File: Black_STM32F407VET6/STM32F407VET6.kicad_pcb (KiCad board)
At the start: 2 copper layers, 100 x 100 mm, 89 parts, among them J1 T0, J10 - HotBed +, J11 Heater0, J12 X-, J13 Y-, J14 Z-, J15 Z+, J16 USB_B, J17 LeftSpi, J18 EXTRAPINS, J19 12Vinput, J2 T1, J20 5VOut, J23 EXP2, J24 LCD2004, J25 Bottom, J26 Right, J28 LIGHTS, J29 Z, J3 TB, J30 Z, J38 X, J39 Y, J4 TC, J41 E0, J43 Heater1, J44 COM, J47 I2C, J48 SPI, J49 SPI, J5 + VIN -, J50 SDIO, J51 Servo, J52 Servo, J53 PowerSelect, J54 Power, J55 PD11, J56 Power, J6 Fan3, J7 Fan2, J8 Fan1, J9 Fan0, Q12 IRLR8726PBF, Q13 IRLR8726PBF, Q14 IRLR8726PBF, Q4 IRLML0030TRPBF, Q6 IRLML0030TRPBF, Q7 IRLML0030TRPBF, Q8 IRLML0030TRPBF, SW1 Boot0, U1 LeftAnalog, U2 Left5V, U3 BuckConvertor, U4 LM2901, U5 AT24CS01-SSHM, U6 LM2901

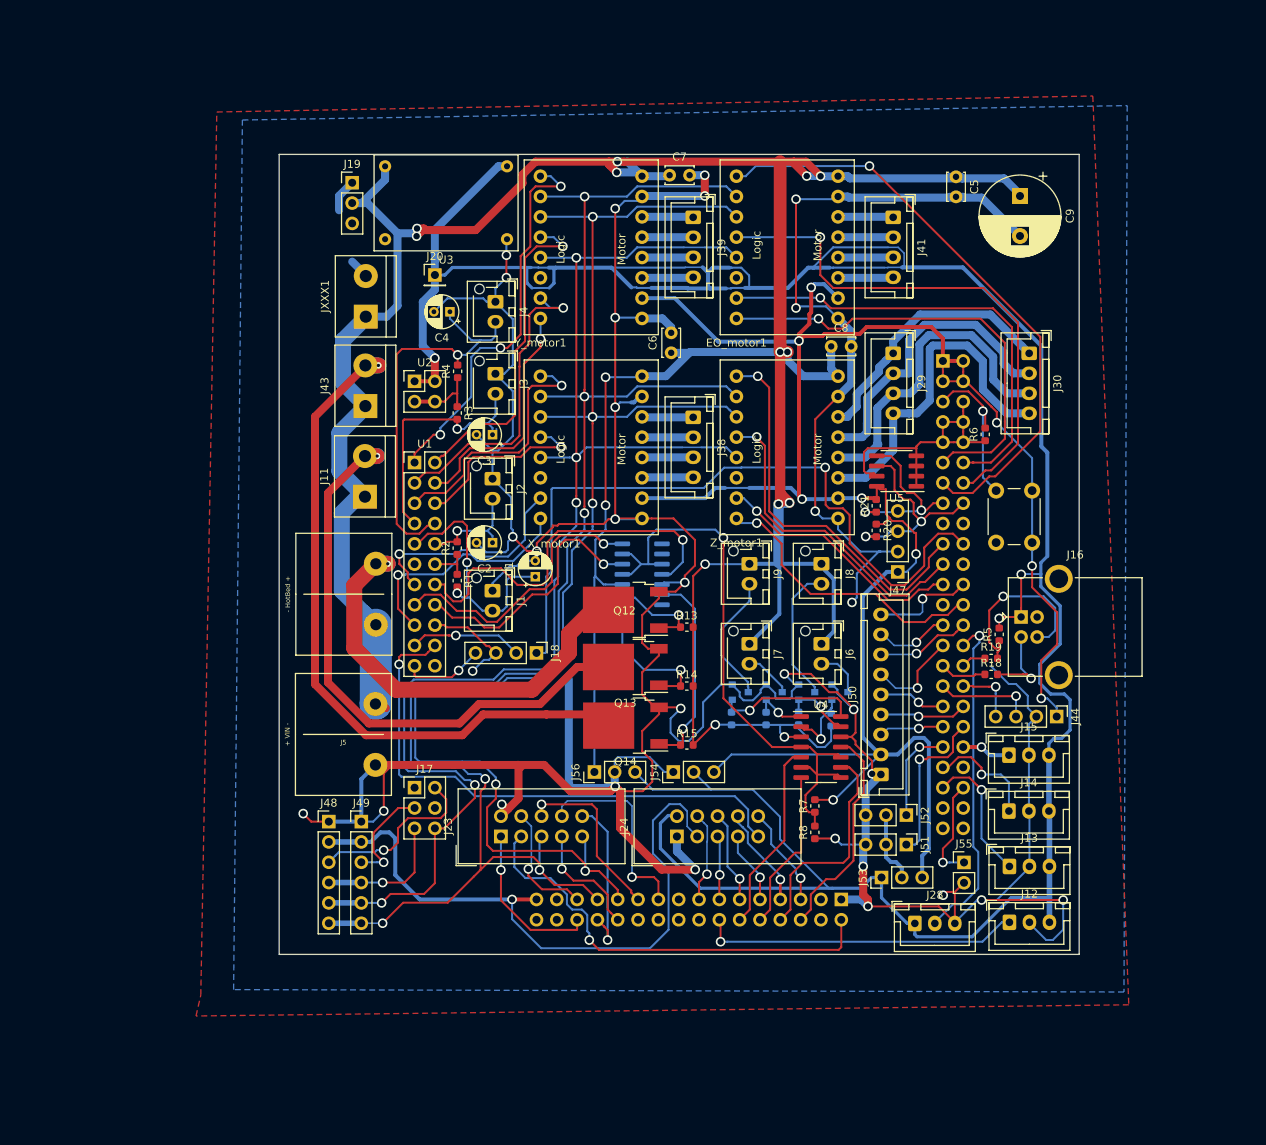
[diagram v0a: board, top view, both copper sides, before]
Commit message: //Forgot to save Fan separated power rail to allow different voltage Moved border to fabrication layer to prepare for milling
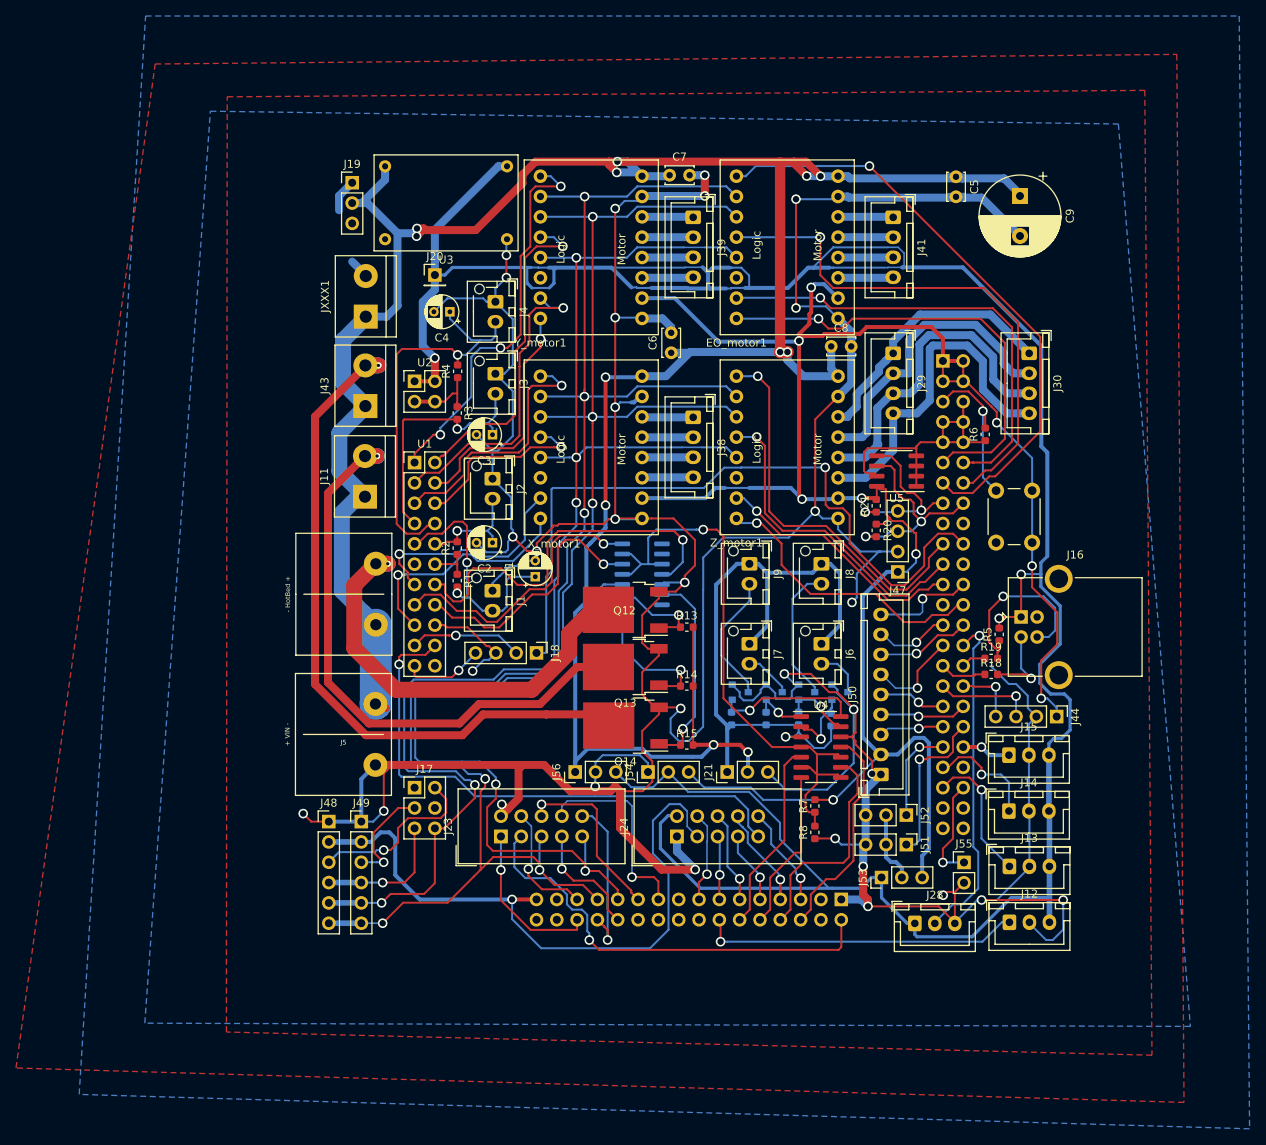
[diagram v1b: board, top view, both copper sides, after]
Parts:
- added J21: Conn_01x03, Connector_PinHeader_2.54mm:PinHeader_1x03_P2.54mm_Vertical, F.Cu at (6.00, 27.2)
- moved J54 3.16 mm to (-3.90, 27.2)
- moved J56 2.40 mm to (-13.0, 27.2)
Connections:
- J6 pad 1: 12V -> FANVoltage
- J7 pad 1: 12V -> FANVoltage
- J8 pad 1: 12V -> FANVoltage
- J9 pad 1: 12V -> FANVoltage
- R10 pad 2: 12V -> FANVoltage
- R11 pad 2: 12V -> FANVoltage
- R12 pad 2: 12V -> FANVoltage
- R9 pad 2: 12V -> FANVoltage
- U4 pad 3: 12V -> FANVoltage
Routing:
- net FANVoltage: track 0.00 -> 83.1 mm, vias 0 -> 1
- net 12V: track 424.2 -> 357.6 mm, vias 15 -> 12
- net GND: track 642.9 -> 673.9 mm
- net 3V3: track 364.0 -> 361.7 mm
- net 5V: track 352.1 -> 353.6 mm
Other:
- board outline removed
